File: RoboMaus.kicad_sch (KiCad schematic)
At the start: 20 parts, among them J1 JST, J2 JST, J3 Color_Pins, J4 Gyro_Pins, Q1 AO3401A, SW1 DSWB01LHGET, U1 AMS1117-3.3

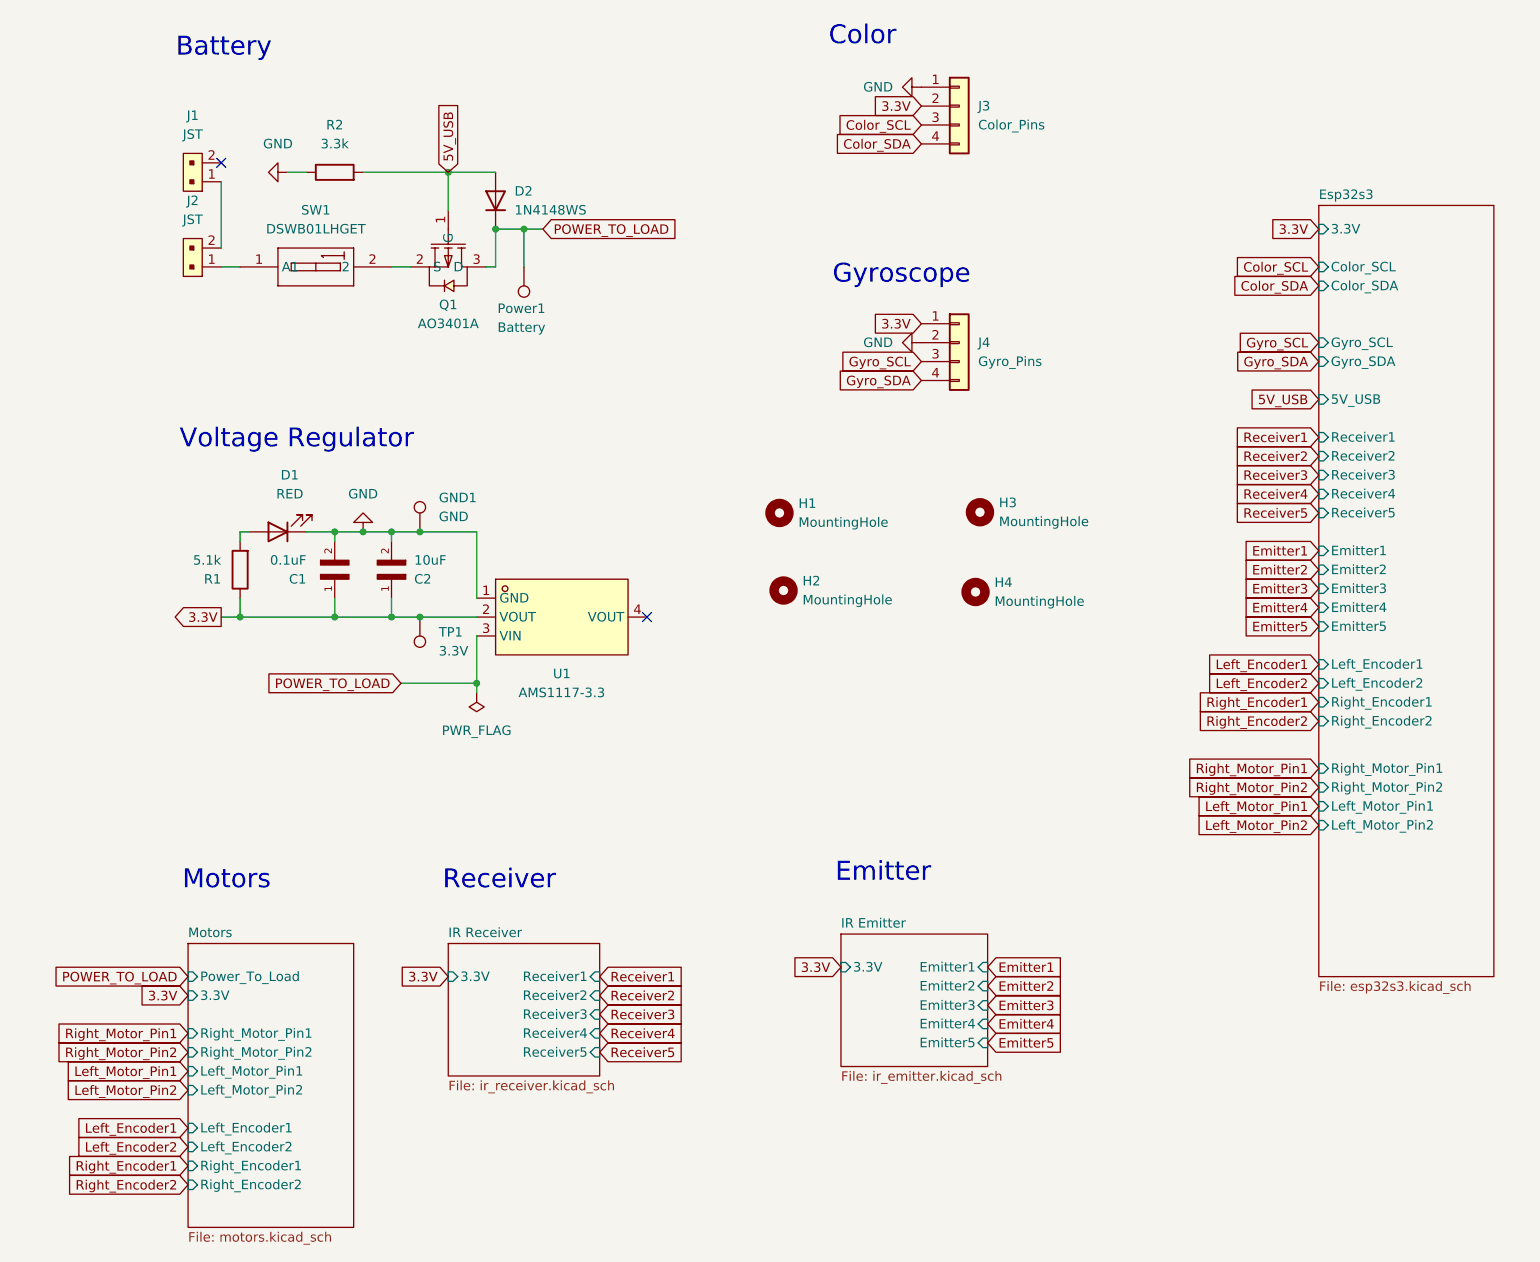
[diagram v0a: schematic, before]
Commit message: schematic: all errors and warnings gone
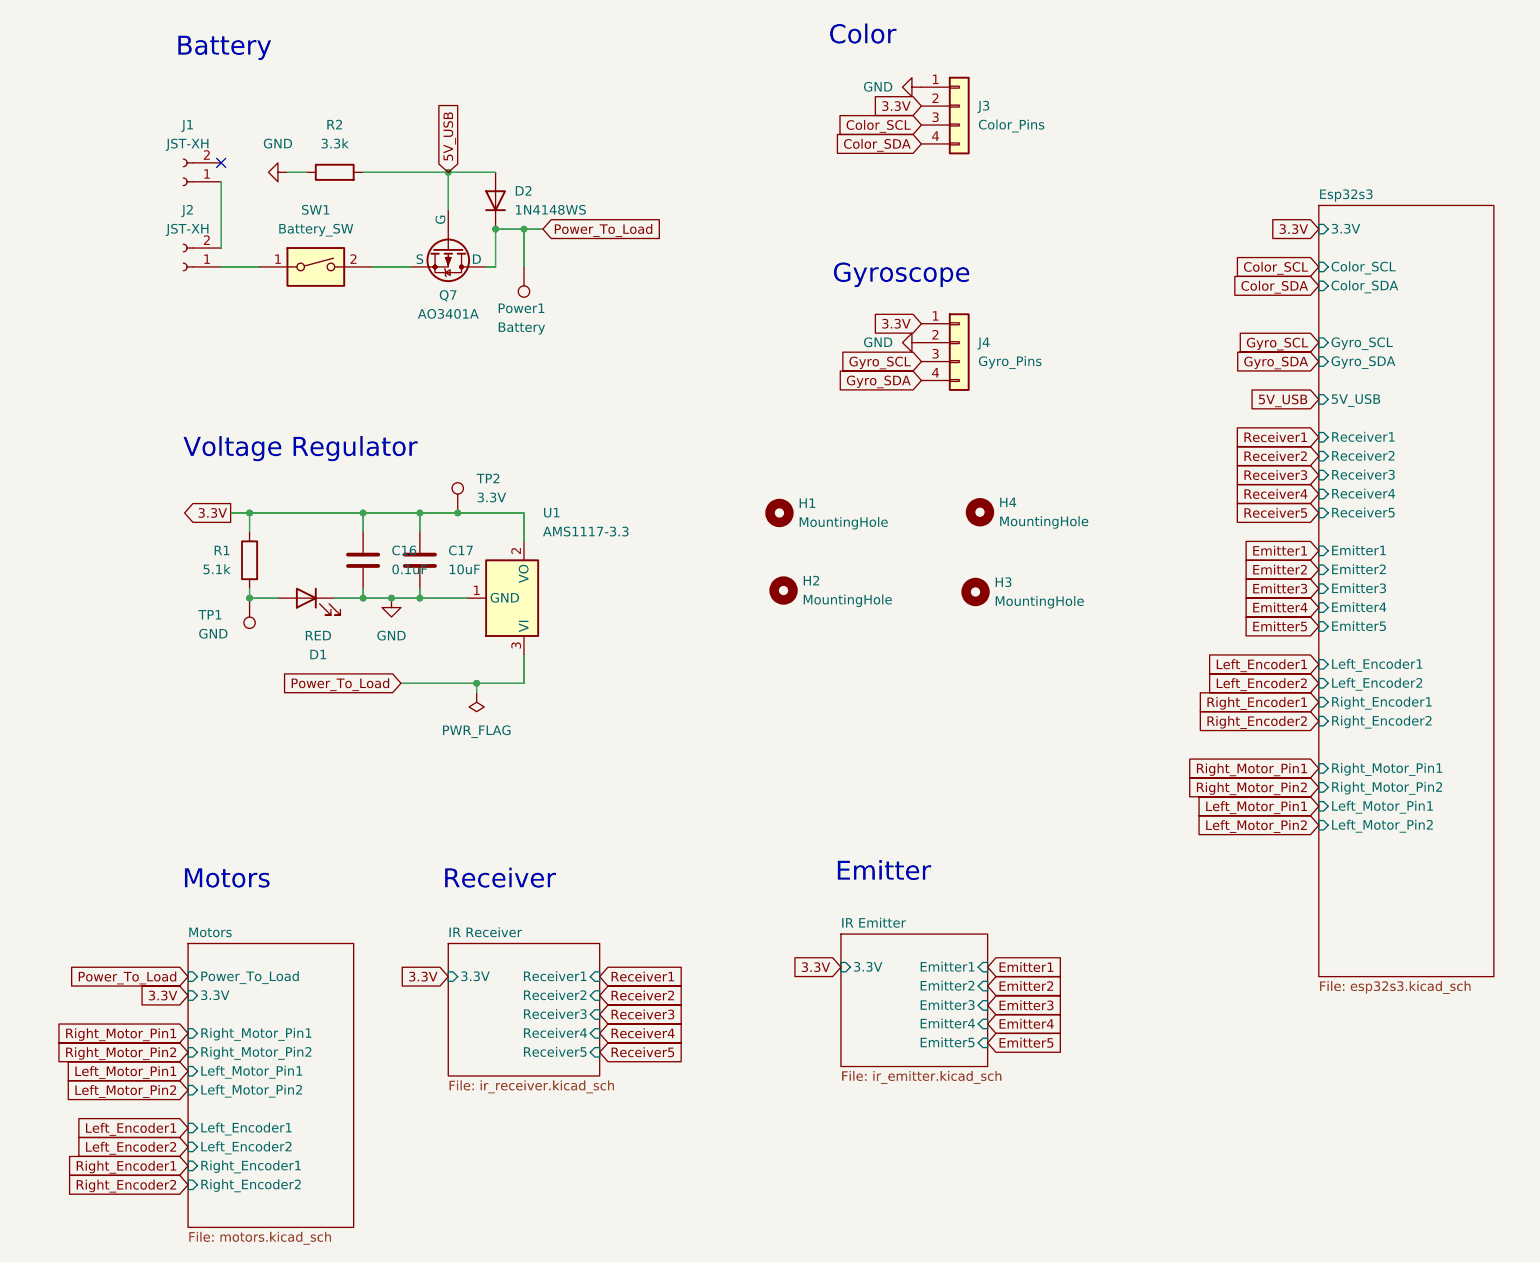
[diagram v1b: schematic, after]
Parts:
- removed C1: 0.1uF, Capacitor_SMD:C_0805_2012Metric_Pad1.18x1.45mm_HandSolder, symbol CL05B104KO5NNNC:CL05B104KO5NNNC
- removed C2: 10uF, Capacitor_SMD:C_0805_2012Metric_Pad1.18x1.45mm_HandSolder, symbol CL21A226MAQNNNE:CL21A226MAQNNNE
- removed GND1: GND, TestPoint:TestPoint_THTPad_2.0x2.0mm_Drill1.0mm, symbol Connector:TestPoint
- removed J1, J2: JST, Connector_JST:JST_XH_B2B-XH-A_1x02_P2.50mm_Vertical, symbol dk_Rectangular-Connectors-Headers-Male-Pins:B2B-PH-K-S_LF__SN_
- removed Q1: AO3401A, easyeda2kicad:SOT-23_L2.9-W1.3-P1.90-LS2.4-BR, symbol Robotastisch:AO3401A
- removed SW1: DSWB01LHGET, easyeda2kicad:SW-TH_DSWB01LHGET, symbol Robotastisch:DSWB01LHGET
- removed U1: AMS1117-3.3, easyeda2kicad:SOT-223-3_L6.5-W3.4-P2.30-LS7.0-BR, symbol Robotastisch:AMS1117-3.3
- added C16: 0.1uF, Capacitor_SMD:C_0805_2012Metric_Pad1.18x1.45mm_HandSolder, symbol Device:C
- added C17: 10uF, Capacitor_SMD:C_0805_2012Metric_Pad1.18x1.45mm_HandSolder, symbol Device:C
- added J1, J2: JST-XH, Connector_JST:JST_XH_B2B-XH-AM_1x02_P2.50mm_Vertical, symbol Connector:Conn_01x02_Socket
- added Q7: AO3401A, Package_TO_SOT_SMD:SOT-23, symbol Simulation_SPICE:PMOS
- added SW1: Battery_SW, Button_Switch_THT:SW_DIP_SPSTx01_Slide_9.78x4.72mm_W7.62mm_P2.54mm, symbol Switch:SW_DIP_x01
- added TP2: 3.3V, TestPoint:TestPoint_THTPad_2.0x2.0mm_Drill1.0mm, symbol Connector:TestPoint
- added U1: AMS1117-3.3, Package_TO_SOT_SMD:SOT-223-3_TabPin2, symbol Regulator_Linear:AMS1117-3.3
- TP1: value 3.3V -> GND
- renumbered H4 to H3, H3 to H4
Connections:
- net 3.3V: now also C16.1, C17.1, TP2.1, U1.2 (VO); no longer TP1.1
- net 5V_USB: now also Q7.2 (G)
- net GND: now also C16.2, C17.2, U1.1 (GND)
- net at D1.2 (A), R1.2: now also TP1.1
- net POWER_TO_LOAD renamed Power_To_Load
- net Power_To_Load: now also Q7.1 (D), U1.3 (VI)
- new net: J2.1 (Pin_1), SW1.1
- new net: J1.1 (Pin_1), J2.2 (Pin_2)
- new net: Q7.3 (S), SW1.2
- no-connect marks 2 -> 1
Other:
- moved on the sheet: D1, R1

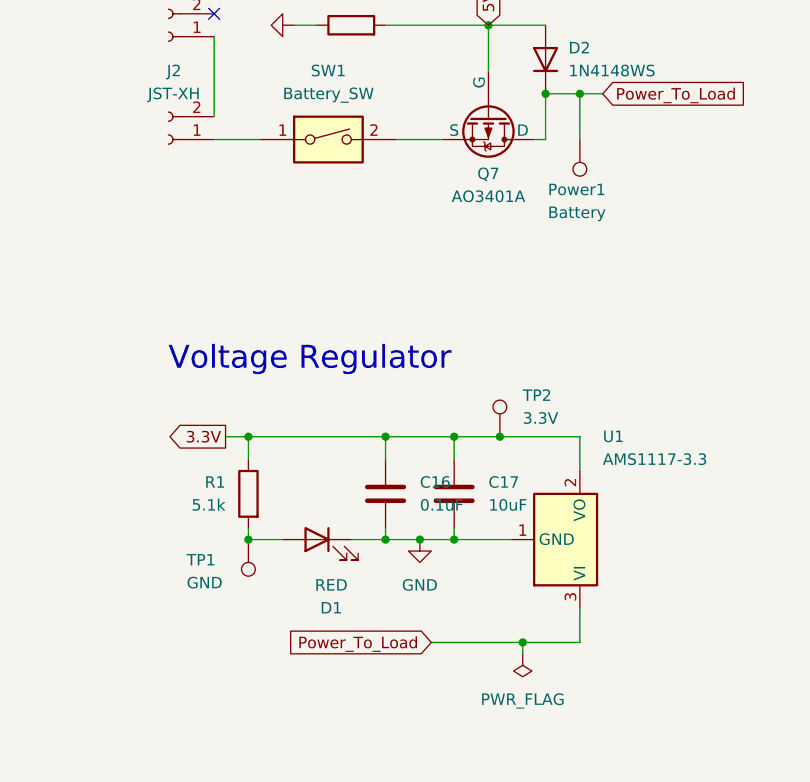
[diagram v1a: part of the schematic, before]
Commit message: pcb: all wired up, most warnings can't be fixed.
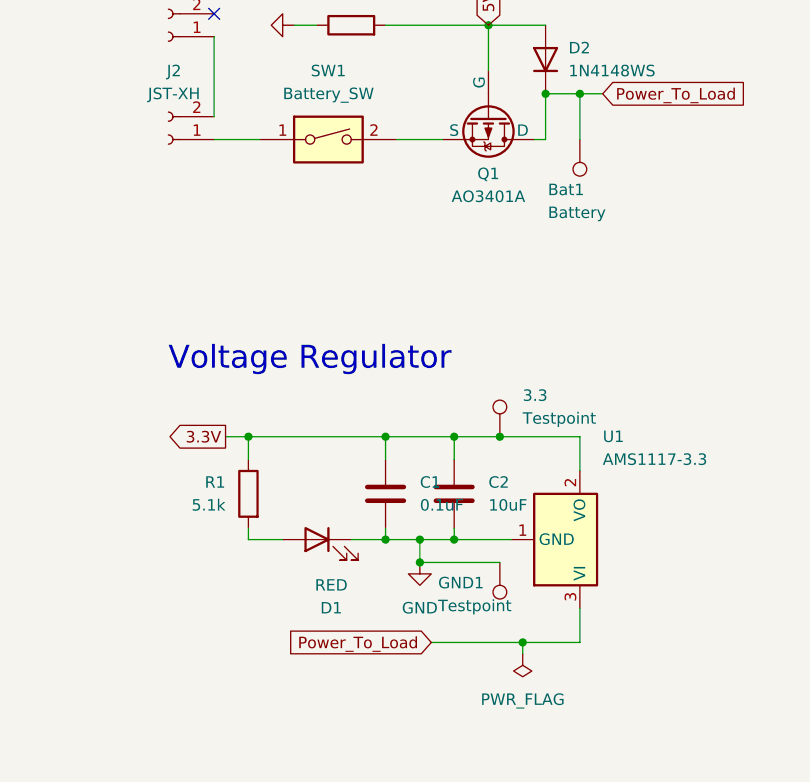
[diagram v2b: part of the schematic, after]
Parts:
- removed TP1: GND, TestPoint:TestPoint_THTPad_2.0x2.0mm_Drill1.0mm, symbol Connector:TestPoint
- added GND1: Testpoint, TestPoint:TestPoint_THTPad_2.0x2.0mm_Drill1.0mm, symbol Connector:TestPoint
- 3.3: renamed from TP2; value 3.3V -> Testpoint
- J1, J2: footprint Connector_JST:JST_XH_B2B-XH-AM_1x02_P2.50mm_Vertical -> Connector_JST:JST_XH_B2B-XH-A_1x02_P2.50mm_Vertical
- renumbered Power1 to Bat1, C16 to C1, C17 to C2, Q7 to Q1
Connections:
- net GND: now also GND1.1
